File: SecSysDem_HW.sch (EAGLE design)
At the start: 49 parts, among them IC1 L7805 5V, Q1 2N3904, T1 MOSFET_NCHANNEL_ENHANCEMENT2N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, T2 MOSFET_NCHANNEL_ENHANCEMENT2N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, T3 MOSFET_NCHANNEL_ENHANCEMENT2N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, U1 XPLAINED_MINI_PINOUT, U2 PCF8574_IO_EXPANDER, U4 FT24C512A, U5 MCP4901-E/SN, X1 C-GRID-06-70553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

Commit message: Finished PCB layout.
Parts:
- added R12, R13, R14, R15, R16, R17, R18: 10k, Luke:RESISTOR0805
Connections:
- net +3V3: now also R12.2, R13.2, R14.2, R15.2, R16.2, R17.2, R18.2
- net KEYPAD_1: now also R12.1
- net KEYPAD_2: now also R13.1
- net KEYPAD_3: now also R14.1
- net KEYPAD_4: now also R15.1
- net KEYPAD_5: now also R16.1
- net KEYPAD_6: now also R17.1
- net KEYPAD_7: now also R18.1
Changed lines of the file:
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@@
 <part name="V2" library="Luke" deviceset="VIA1" device="" value="32k"/>
 <part name="V10" library="Luke" deviceset="VIA1" device="" value="SQW"/>
+<part name="R12" library="Luke" deviceset="RESISTOR" device="0805" value="10k"/>
+<part name="R13" library="Luke" deviceset="RESISTOR" device="0805" value="10k"/>
+<part name="R14" library="Luke" deviceset="RESISTOR" device="0805" value="10k"/>
+<part name="R15" library="Luke" deviceset="RESISTOR" device="0805" value="10k"/>
+<part name="R16" library="Luke" deviceset="RESISTOR" device="0805" value="10k"/>
+<part name="R17" library="Luke" deviceset="RESISTOR" device="0805" value="10k"/>
+<part name="R18" library="Luke" deviceset="RESISTOR" device="0805" value="10k"/>
+<part name="+3V14" library="supply1" deviceset="+3V3" device=""/>
 </parts>
 <sheets>
@@
 <instance part="V2" gate="G$1" x="208.28" y="66.04" rot="R180"/>
 <instance part="V10" gate="G$1" x="208.28" y="68.58" rot="R180"/>
+<instance part="R12" gate="G$1" x="63.5" y="55.88" rot="R90"/>
+<instance part="R13" gate="G$1" x="66.04" y="55.88" rot="R90"/>
+<instance part="R14" gate="G$1" x="68.58" y="55.88" rot="R90"/>
+<instance part="R15" gate="G$1" x="71.12" y="55.88" rot="R90"/>
+<instance part="R16" gate="G$1" x="73.66" y="55.88" rot="R90"/>
+<instance part="R17" gate="G$1" x="76.2" y="55.88" rot="R90"/>
+<instance part="R18" gate="G$1" x="78.74" y="55.88" rot="R90"/>
+<instance part="+3V14" gate="G$1" x="58.42" y="63.5" rot="R90"/>
 </instances>
 <busses>
@@
 <pinref part="+3V13" gate="G$1" pin="+3V3"/>
 </segment>
+<segment>
+<pinref part="+3V14" gate="G$1" pin="+3V3"/>
+<pinref part="R12" gate="G$1" pin="2"/>
+<wire x1="60.96" y1="63.5" x2="63.5" y2="63.5" width="0.1524" layer="91"/>
+<wire x1="63.5" y1="63.5" x2="63.5" y2="60.96" width="0.1524" layer="91"/>
+<pinref part="R13" gate="G$1" pin="2"/>
+<wire x1="63.5" y1="63.5" x2="66.04" y2="63.5" width="0.1524" layer="91"/>
+<wire x1="66.04" y1="63.5" x2="66.04" y2="60.96" width="0.1524" layer="91"/>
+<junction x="63.5" y="63.5"/>
+<pinref part="R14" gate="G$1" pin="2"/>
+<wire x1="66.04" y1="63.5" x2="68.58" y2="63.5" width="0.1524" layer="91"/>
+<wire x1="68.58" y1="63.5" x2="68.58" y2="60.96" width="0.1524" layer="91"/>
+<junction x="66.04" y="63.5"/>
+<pinref part="R15" gate="G$1" pin="2"/>
+<wire x1="68.58" y1="63.5" x2="71.12" y2="63.5" width="0.1524" layer="91"/>
+<wire x1="71.12" y1="63.5" x2="71.12" y2="60.96" width="0.1524" layer="91"/>
+<junction x="68.58" y="63.5"/>
+<pinref part="R16" gate="G$1" pin="2"/>
+<wire x1="71.12" y1="63.5" x2="73.66" y2="63.5" width="0.1524" layer="91"/>
+<wire x1="73.66" y1="63.5" x2="73.66" y2="60.96" width="0.1524" layer="91"/>
+<junction x="71.12" y="63.5"/>
+<pinref part="R17" gate="G$1" pin="2"/>
+<wire x1="73.66" y1="63.5" x2="76.2" y2="63.5" width="0.1524" layer="91"/>
+<wire x1="76.2" y1="63.5" x2="76.2" y2="60.96" width="0.1524" layer="91"/>
+<junction x="73.66" y="63.5"/>
+<pinref part="R18" gate="G$1" pin="2"/>
+<wire x1="76.2" y1="63.5" x2="78.74" y2="63.5" width="0.1524" layer="91"/>
+<wire x1="78.74" y1="63.5" x2="78.74" y2="60.96" width="0.1524" layer="91"/>
+<junction x="76.2" y="63.5"/>
+</segment>
 </net>
 <net name="PHOTORESISTOR" class="0">
 <segment>
 <pinref part="U1" gate="G$1" pin="H5"/>
-<wire x1="106.68" y1="60.96" x2="96.52" y2="60.96" width="0.1524" layer="91"/>
-<label x="96.52" y="60.96" size="1.27" layer="95" rot="MR0" xref="yes"/>
+<wire x1="106.68" y1="60.96" x2="99.06" y2="60.96" width="0.1524" layer="91"/>
+<label x="99.06" y="60.96" size="1.27" layer="95" rot="MR0" xref="yes"/>
 </segment>
 <segment>
@@
 <segment>
 <wire x1="60.96" y1="38.1" x2="71.12" y2="38.1" width="0.1524" layer="91"/>
-<label x="71.12" y="38.1" size="1.27" layer="95" xref="yes"/>
+<label x="83.82" y="38.1" size="1.27" layer="95" xref="yes"/>
 <pinref part="U2" gate="G$1" pin="P4"/>
+<pinref part="R15" gate="G$1" pin="1"/>
+<wire x1="71.12" y1="38.1" x2="83.82" y2="38.1" width="0.1524" layer="91"/>
+<wire x1="71.12" y1="50.8" x2="71.12" y2="38.1" width="0.1524" layer="91"/>
+<junction x="71.12" y="38.1"/>
 </segment>
 <segment>
@@
 <net name="KEYPAD_5" class="0">
 <segment>
-<wire x1="60.96" y1="35.56" x2="71.12" y2="35.56" width="0.1524" layer="91"/>
-<label x="71.12" y="35.56" size="1.27" layer="95" xref="yes"/>
+<wire x1="60.96" y1="35.56" x2="73.66" y2="35.56" width="0.1524" layer="91"/>
+<label x="83.82" y="35.56" size="1.27" layer="95" xref="yes"/>
 <pinref part="U2" gate="G$1" pin="P5"/>
+<pinref part="R16" gate="G$1" pin="1"/>
+<wire x1="73.66" y1="35.56" x2="83.82" y2="35.56" width="0.1524" layer="91"/>
+<wire x1="73.66" y1="50.8" x2="73.66" y2="35.56" width="0.1524" layer="91"/>
+<junction x="73.66" y="35.56"/>
 </segment>
 <segment>
@@
 <net name="KEYPAD_6" class="0">
 <segment>
-<wire x1="60.96" y1="33.02" x2="71.12" y2="33.02" width="0.1524" layer="91"/>
-<label x="71.12" y="33.02" size="1.27" layer="95" xref="yes"/>
+<wire x1="60.96" y1="33.02" x2="76.2" y2="33.02" width="0.1524" layer="91"/>
+<label x="83.82" y="33.02" size="1.27" layer="95" xref="yes"/>
 <pinref part="U2" gate="G$1" pin="P6"/>
+<pinref part="R17" gate="G$1" pin="1"/>
+<wire x1="76.2" y1="33.02" x2="83.82" y2="33.02" width="0.1524" layer="91"/>
+<wire x1="76.2" y1="50.8" x2="76.2" y2="33.02" width="0.1524" layer="91"/>
+<junction x="76.2" y="33.02"/>
 </segment>
 <segment>
@@
 <net name="KEYPAD_7" class="0">
 <segment>
-<wire x1="60.96" y1="30.48" x2="71.12" y2="30.48" width="0.1524" layer="91"/>
-<label x="71.12" y="30.48" size="1.27" layer="95" xref="yes"/>
+<wire x1="60.96" y1="30.48" x2="78.74" y2="30.48" width="0.1524" layer="91"/>
+<label x="83.82" y="30.48" size="1.27" layer="95" xref="yes"/>
 <pinref part="U2" gate="G$1" pin="P7"/>
+<pinref part="R18" gate="G$1" pin="1"/>
+<wire x1="78.74" y1="30.48" x2="83.82" y2="30.48" width="0.1524" layer="91"/>
+<wire x1="78.74" y1="50.8" x2="78.74" y2="30.48" width="0.1524" layer="91"/>
+<junction x="78.74" y="30.48"/>
 </segment>
 <segment>
@@
 <net name="KEYPAD_1" class="0">
 <segment>
-<wire x1="71.12" y1="45.72" x2="60.96" y2="45.72" width="0.1524" layer="91"/>
-<label x="71.12" y="45.72" size="1.27" layer="95" rot="MR180" xref="yes"/>
+<wire x1="83.82" y1="45.72" x2="63.5" y2="45.72" width="0.1524" layer="91"/>
+<label x="83.82" y="45.72" size="1.27" layer="95" rot="MR180" xref="yes"/>
 <pinref part="U2" gate="G$1" pin="P1"/>
+<pinref part="R12" gate="G$1" pin="1"/>
+<wire x1="63.5" y1="45.72" x2="60.96" y2="45.72" width="0.1524" layer="91"/>
+<wire x1="63.5" y1="50.8" x2="63.5" y2="45.72" width="0.1524" layer="91"/>
+<junction x="63.5" y="45.72"/>
 </segment>
 <segment>
@@
 <net name="KEYPAD_2" class="0">
 <segment>
-<wire x1="71.12" y1="43.18" x2="60.96" y2="43.18" width="0.1524" layer="91"/>
-<label x="71.12" y="43.18" size="1.27" layer="95" rot="MR180" xref="yes"/>
+<wire x1="83.82" y1="43.18" x2="66.04" y2="43.18" width="0.1524" layer="91"/>
+<label x="83.82" y="43.18" size="1.27" layer="95" rot="MR180" xref="yes"/>
 <pinref part="U2" gate="G$1" pin="P2"/>
+<pinref part="R13" gate="G$1" pin="1"/>
+<wire x1="66.04" y1="43.18" x2="60.96" y2="43.18" width="0.1524" layer="91"/>
+<wire x1="66.04" y1="50.8" x2="66.04" y2="43.18" width="0.1524" layer="91"/>
+<junction x="66.04" y="43.18"/>
 </segment>
 <segment>
@@
 <net name="KEYPAD_3" class="0">
 <segment>
-<wire x1="71.12" y1="40.64" x2="60.96" y2="40.64" width="0.1524" layer="91"/>
-<label x="71.12" y="40.64" size="1.27" layer="95" rot="MR180" xref="yes"/>
+<wire x1="83.82" y1="40.64" x2="68.58" y2="40.64" width="0.1524" layer="91"/>
+<label x="83.82" y="40.64" size="1.27" layer="95" rot="MR180" xref="yes"/>
 <pinref part="U2" gate="G$1" pin="P3"/>
+<pinref part="R14" gate="G$1" pin="1"/>
+<wire x1="68.58" y1="40.64" x2="60.96" y2="40.64" width="0.1524" layer="91"/>
+<wire x1="68.58" y1="50.8" x2="68.58" y2="40.64" width="0.1524" layer="91"/>
+<junction x="68.58" y="40.64"/>
 </segment>
 <segment>
@@
 <net name="BELL_RINGER" class="0">
 <segment>
-<wire x1="60.96" y1="48.26" x2="71.12" y2="48.26" width="0.1524" layer="91"/>
-<label x="71.12" y="48.26" size="1.27" layer="95" xref="yes"/>
+<wire x1="60.96" y1="48.26" x2="83.82" y2="48.26" width="0.1524" layer="91"/>
+<label x="83.82" y="48.26" size="1.27" layer="95" xref="yes"/>
 <pinref part="U2" gate="G$1" pin="P0"/>
 </segment>

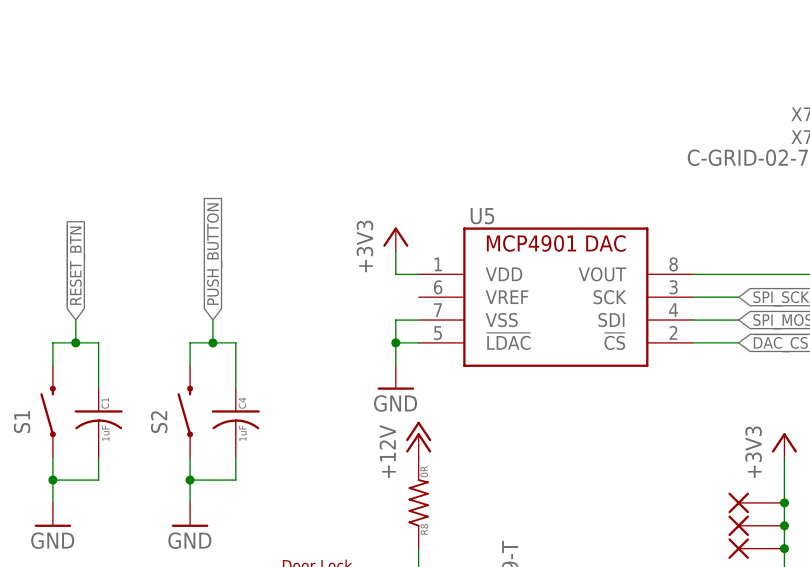
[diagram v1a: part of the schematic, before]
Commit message: Refinished board layout with silkscreen.
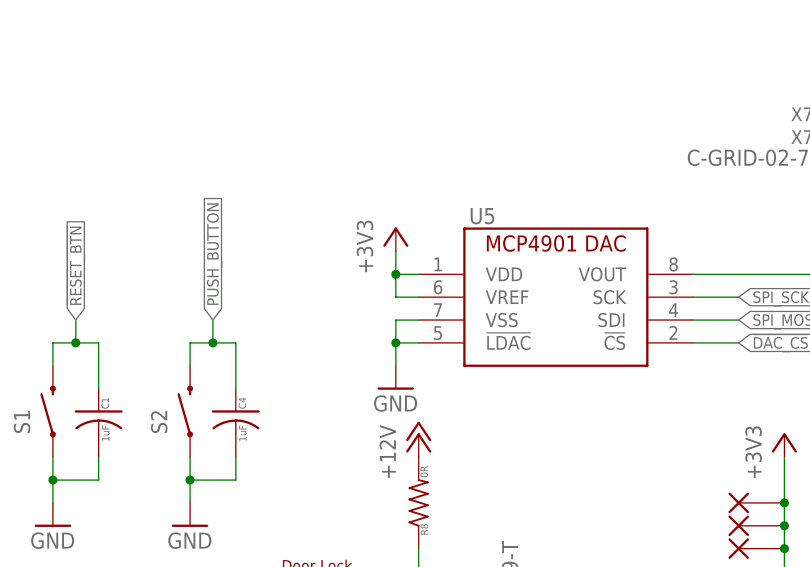
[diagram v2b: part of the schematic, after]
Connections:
- net +3V3: now also U5.VREF
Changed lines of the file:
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@@
 <pinref part="+3V7" gate="G$1" pin="+3V3"/>
 <pinref part="U5" gate="G$1" pin="VDD"/>
+<pinref part="U5" gate="G$1" pin="VREF"/>
+<wire x1="50.8" y1="121.92" x2="48.26" y2="121.92" width="0.1524" layer="91"/>
+<wire x1="48.26" y1="121.92" x2="48.26" y2="124.46" width="0.1524" layer="91"/>
+<junction x="48.26" y="124.46"/>
 </segment>
 <segment>

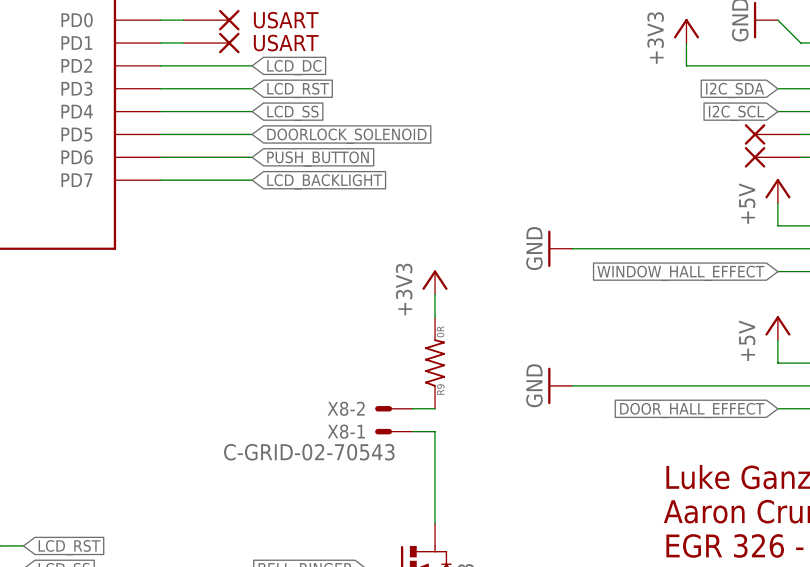
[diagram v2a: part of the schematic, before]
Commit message: Change bell to +5v
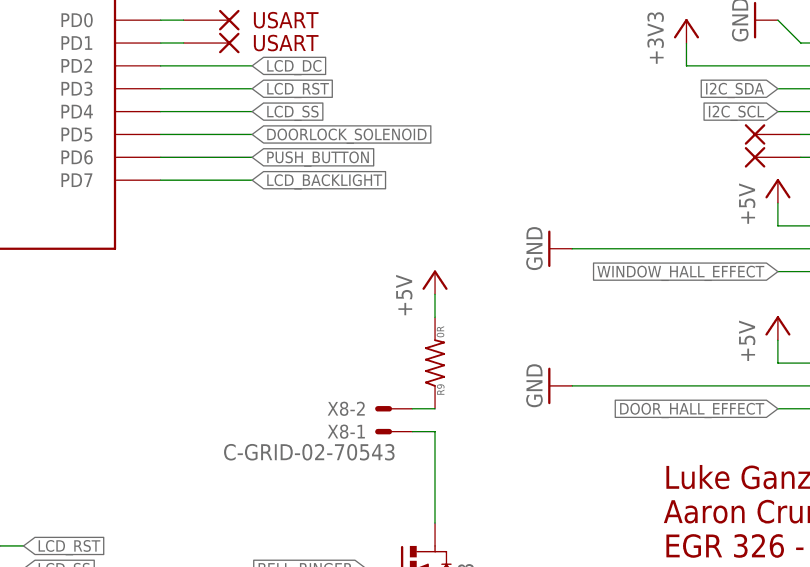
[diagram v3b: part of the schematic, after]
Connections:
- net +3V3: no longer R9.2
- net +5V: now also R9.2
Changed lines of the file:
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@@
 <part name="X8" library="con-molex" deviceset="C-GRID-02" device="-70543"/>
 <part name="R9" library="Luke" deviceset="RESISTOR" device="0805" value="0R"/>
-<part name="+3V10" library="supply1" deviceset="+3V3" device=""/>
 <part name="V3" library="Luke" deviceset="VIA1" device="" value="TXD"/>
 <part name="V4" library="Luke" deviceset="VIA1" device="" value="RXD"/>
@@
 <part name="R18" library="Luke" deviceset="RESISTOR" device="0805" value="10k"/>
 <part name="+3V14" library="supply1" deviceset="+3V3" device=""/>
+<part name="P+8" library="supply1" deviceset="+5V" device=""/>
 </parts>
 <sheets>
@@
 <instance part="X8" gate="-1" x="167.64" y="35.56" rot="R180"/>
 <instance part="R9" gate="G$1" x="172.72" y="43.18" rot="R90"/>
-<instance part="+3V10" gate="G$1" x="172.72" y="53.34"/>
 <instance part="V3" gate="G$1" x="149.86" y="81.28"/>
 <instance part="V4" gate="G$1" x="149.86" y="78.74"/>
@@
 <instance part="R18" gate="G$1" x="78.74" y="55.88" rot="R90"/>
 <instance part="+3V14" gate="G$1" x="58.42" y="63.5" rot="R90"/>
+<instance part="P+8" gate="1" x="172.72" y="53.34"/>
 </instances>
 <busses>
@@
 <pinref part="P+7" gate="1" pin="+5V"/>
 <pinref part="JP4" gate="G$1" pin="3"/>
+</segment>
+<segment>
+<pinref part="R9" gate="G$1" pin="2"/>
+<wire x1="172.72" y1="50.8" x2="172.72" y2="48.26" width="0.1524" layer="91"/>
+<pinref part="P+8" gate="1" pin="+5V"/>
 </segment>
 </net>
@@
 </segment>
 <segment>
-<pinref part="R9" gate="G$1" pin="2"/>
-<pinref part="+3V10" gate="G$1" pin="+3V3"/>
-<wire x1="172.72" y1="50.8" x2="172.72" y2="48.26" width="0.1524" layer="91"/>
-</segment>
-<segment>

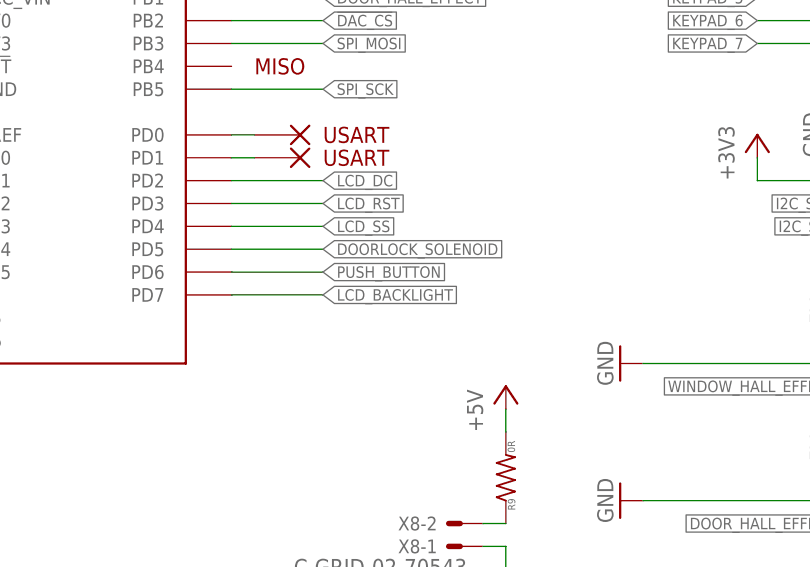
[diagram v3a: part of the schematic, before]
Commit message: Changed the pins so that the backlight is on PD6 instead of PD7 for pwm.
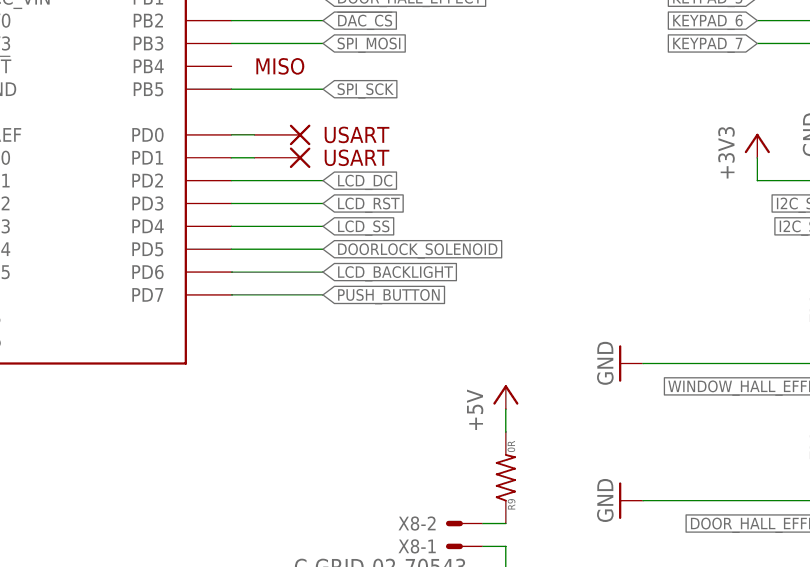
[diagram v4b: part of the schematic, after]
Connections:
- net LCD_BACKLIGHT: now also U1.PD6; no longer U1.PD7
- net PUSH_BUTTON: now also U1.PD7; no longer U1.PD6
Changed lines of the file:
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@@
 <net name="LCD_BACKLIGHT" class="0">
 <segment>
-<wire x1="142.24" y1="63.5" x2="152.4" y2="63.5" width="0.1524" layer="91"/>
-<label x="152.4" y="63.5" size="1.27" layer="95" xref="yes"/>
-<pinref part="U1" gate="G$1" pin="PD7"/>
+<wire x1="142.24" y1="66.04" x2="152.4" y2="66.04" width="0.1524" layer="91"/>
+<label x="152.4" y="66.04" size="1.27" layer="95" xref="yes"/>
+<pinref part="U1" gate="G$1" pin="PD6"/>
 </segment>
 <segment>
@@
 <pinref part="R10" gate="G$1" pin="1"/>
 <wire x1="55.88" y1="15.24" x2="53.34" y2="15.24" width="0.1524" layer="91"/>
-</segment>
-</net>
-<net name="PUSH_BUTTON" class="0">
-<segment>
-<wire x1="142.24" y1="66.04" x2="152.4" y2="66.04" width="0.1524" layer="91"/>
-<label x="152.4" y="66.04" size="1.27" layer="95" xref="yes"/>
-<pinref part="U1" gate="G$1" pin="PD6"/>
-</segment>
-<segment>
-<pinref part="S2" gate="G$1" pin="2"/>
-<pinref part="C4" gate="G$1" pin="POS"/>
-<wire x1="25.4" y1="116.84" x2="25.4" y2="114.3" width="0.1524" layer="91"/>
-<wire x1="30.48" y1="111.76" x2="30.48" y2="116.84" width="0.1524" layer="91"/>
-<wire x1="30.48" y1="116.84" x2="27.94" y2="116.84" width="0.1524" layer="91"/>
-<wire x1="27.94" y1="116.84" x2="25.4" y2="116.84" width="0.1524" layer="91"/>
-<wire x1="27.94" y1="116.84" x2="27.94" y2="119.38" width="0.1524" layer="91"/>
-<junction x="27.94" y="116.84"/>
-<label x="27.94" y="119.38" size="1.27" layer="95" rot="R90" xref="yes"/>
 </segment>
 </net>
@@
 </segment>
 </net>
+<net name="PUSH_BUTTON" class="0">
+<segment>
+<pinref part="S2" gate="G$1" pin="2"/>
+<pinref part="C4" gate="G$1" pin="POS"/>
+<wire x1="25.4" y1="116.84" x2="25.4" y2="114.3" width="0.1524" layer="91"/>
+<wire x1="30.48" y1="111.76" x2="30.48" y2="116.84" width="0.1524" layer="91"/>
+<wire x1="30.48" y1="116.84" x2="27.94" y2="116.84" width="0.1524" layer="91"/>
+<wire x1="27.94" y1="116.84" x2="25.4" y2="116.84" width="0.1524" layer="91"/>
+<wire x1="27.94" y1="116.84" x2="27.94" y2="119.38" width="0.1524" layer="91"/>
+<junction x="27.94" y="116.84"/>
+<label x="27.94" y="119.38" size="1.27" layer="95" rot="R90" xref="yes"/>
+</segment>
+<segment>
+<wire x1="142.24" y1="63.5" x2="152.4" y2="63.5" width="0.1524" layer="91"/>
+<label x="152.4" y="63.5" size="1.27" layer="95" xref="yes"/>
+<pinref part="U1" gate="G$1" pin="PD7"/>
+</segment>
+</net>

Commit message: Added text
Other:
- note added: "Doorlock draws 550mA at (255/255) 100% duty cycle and 90mA at (30/255) duty cycle."
- note added: "OC0A"
- note added: "OC0B"
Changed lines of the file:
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@@
 <text x="152.4" y="81.28" size="1.778" layer="94" align="center-left">USART</text>
 <text x="144.78" y="88.9" size="1.778" layer="94" align="center-left">MISO</text>
+<text x="129.54" y="68.58" size="0.8128" layer="97" rot="R180" align="center-left">OC0B</text>
+<text x="129.54" y="66.04" size="0.8128" layer="97" rot="R180" align="center-left">OC0A</text>
+<text x="48.26" y="81.28" size="0.8128" layer="97" rot="R180" align="center-left">Doorlock draws 550mA at (255/255) 100% duty cycle
+and 90mA at (30/255) duty cycle.</text>
 </plain>
 <instances>
